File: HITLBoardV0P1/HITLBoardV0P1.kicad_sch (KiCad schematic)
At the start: 2 parts

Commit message: ADD SOLENOID VALVE CIRCUIT
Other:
- added sheet Solenoid-Valve (SolenoidValve.kicad_sch)
- added sheet Solenoid-Valve1 (SolenoidValve.kicad_sch)
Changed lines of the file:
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@@
 	(wire
 		(pts
+			(xy 513.08 213.36) (xy 537.21 213.36)
+		)
+		(stroke
+			(width 0)
+			(type default)
+		)
+	)
+	(wire
+		(pts
+			(xy 226.06 165.1) (xy 248.92 165.1)
+		)
+		(stroke
+			(width 0)
+			(type default)
+		)
+	)
+	(wire
+		(pts
 			(xy 381 317.5) (xy 403.86 317.5)
 		)
@@
 	(wire
 		(pts
+			(xy 167.64 209.55) (xy 187.96 209.55)
+		)
+		(stroke
+			(width 0)
+			(type default)
+		)
+	)
+	(wire
+		(pts
 			(xy 387.35 49.53) (xy 406.4 49.53)
 		)
@@
 	(wire
 		(pts
+			(xy 93.98 133.35) (xy 114.3 133.35)
+		)
+		(stroke
+			(width 0)
+			(type default)
+		)
+	)
+	(wire
+		(pts
 			(xy 290.83 303.53) (xy 314.96 303.53)
 		)
@@
 	(wire
 		(pts
+			(xy 226.06 209.55) (xy 248.92 209.55)
+		)
+		(stroke
+			(width 0)
+			(type default)
+		)
+	)
+	(wire
+		(pts
 			(xy 433.07 68.58) (xy 457.2 68.58)
 		)
@@
 	(wire
 		(pts
+			(xy 167.64 165.1) (xy 187.96 165.1)
+		)
+		(stroke
+			(width 0)
+			(type default)
+		)
+	)
+	(wire
+		(pts
 			(xy 130.81 330.2) (xy 149.86 330.2)
 		)
@@
 		)
 	)
+	(label "SV_ON_1"
+		(at 519.43 213.36 0)
+		(effects
+			(font
+				(size 1.27 1.27)
+			)
+			(justify left bottom)
+		)
+	)
 	(label "LAN_WAKE_1"
 		(at 438.15 73.66 0)
@@
 		)
 	)
+	(label "SV_EN_1"
+		(at 171.45 209.55 0)
+		(effects
+			(font
+				(size 1.27 1.27)
+			)
+			(justify left bottom)
+		)
+	)
 	(label "LAN1_RESET_N"
 		(at 307.34 53.34 0)
@@
 		)
 	)
+	(label "SV_EN_1"
+		(at 97.79 133.35 0)
+		(effects
+			(font
+				(size 1.27 1.27)
+			)
+			(justify left bottom)
+		)
+	)
 	(label "DAC_CLR3"
 		(at 476.25 321.31 90)
@@
 		)
 	)
+	(label "SV_ON_1"
+		(at 232.41 209.55 0)
+		(effects
+			(font
+				(size 1.27 1.27)
+			)
+			(justify left bottom)
+		)
+	)
 	(label "RPI_I2C_SCL"
 		(at 440.69 209.55 0)
@@
 		)
 	)
+	(label "SV_ON_1"
+		(at 232.41 165.1 0)
+		(effects
+			(font
+				(size 1.27 1.27)
+			)
+			(justify left bottom)
+		)
+	)
 	(label "RPI_SPI1_MOSI"
 		(at 215.9 340.36 0)
@@
 		)
 	)
+	(label "SV_EN_1"
+		(at 171.45 165.1 0)
+		(effects
+			(font
+				(size 1.27 1.27)
+			)
+			(justify left bottom)
+		)
+	)
 	(label "TMDX_SPI1_CS0_N"
 		(at 99.06 69.85 0)
@@
 	)
 	(sheet
+		(at 187.96 146.05)
+		(size 38.1 36.83)
+		(exclude_from_sim no)
+		(in_bom yes)
+		(on_board yes)
+		(dnp no)
+		(fields_autoplaced yes)
+		(stroke
+			(width 0.1524)
+			(type solid)
+		)
+		(fill
+			(color 0 0 0 0)
+		)
+		(property "Sheetname" "Solenoid-Valve"
+			(at 187.96 145.3384 0)
+			(show_name no)
+			(do_not_autoplace no)
+			(effects
+				(font
+					(size 1.27 1.27)
+				)
+				(justify left bottom)
+			)
+		)
+		(property "Sheetfile" "SolenoidValve.kicad_sch"
+			(at 187.96 183.4646 0)
+			(show_name no)
+			(do_not_autoplace no)
+			(effects
+				(font
+					(size 1.27 1.27)
+				)
+				(justify left top)
+			)
+		)
+		(pin "SV_EN_3V3" input
+			(at 187.96 165.1 180)
+			(effects
+				(font
+					(size 1.27 1.27)
+				)
+				(justify left)
+			)
+		)
+		(pin "SV_ON_3V3" input
+			(at 226.06 165.1 0)
+			(effects
+				(font
+					(size 1.27 1.27)
+				)
+				(justify right)
+			)
+		)
+		(instances
+			(project "HITLBoardV0P1"
+				(path "/ef043e91-6391-40b5-b326-2e3f2f5d4c07"
+					(page "14")
+				)
+			)
+		)
+	)
+	(sheet
 		(at 382.27 328.93)
 		(size 129.54 38.1)
@@
 				)
 			)
+		)
+	)
+	(sheet
+		(at 187.96 190.5)
+		(size 38.1 36.83)
+		(exclude_from_sim no)
+		(in_bom yes)
+		(on_board yes)
+		(dnp no)
+		(fields_autoplaced yes)
+		(stroke
+			(width 0.1524)
+			(type solid)
+		)
+		(fill
+			(color 0 0 0 0)
+		)
+		(property "Sheetname" "Solenoid-Valve1"
+			(at 187.96 189.7884 0)
+			(show_name no)
+			(do_not_autoplace no)
+			(effects
+				(font
+					(size 1.27 1.27)
+				)
+				(justify left bottom)
+			)
+		)
+		(property "Sheetfile" "SolenoidValve.kicad_sch"
+			(at 187.96 227.9146 0)
+			(show_name no)
+			(do_not_autoplace no)
+			(effects
+				(font
+					(size 1.27 1.27)
+				)
+				(justify left top)
+			)
+		)
+		(pin "SV_EN_3V3" input
+			(at 187.96 209.55 180)
+			(effects
+				(font
+					(size 1.27 1.27)
+				)
+				(justify left)
+			)
+		)
+		(pin "SV_ON_3V3" input
+			(at 226.06 209.55 0)
+			(effects
+				(font
+					(size 1.27 1.27)
+				)
+				(justify right)
+			)
+		)
+		(instances
+			(project "HITLBoardV0P1"
+				(path "/ef043e91-6391-40b5-b326-2e3f2f5d4c07"
+					(page "15")
+				)
+			)

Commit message: add debug LEDs and reset_n button for system reset
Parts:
- added R83: 10K, Resistor_SMD:R_01005_0402Metric, symbol Device:R_US
- added SW1: SW_Push, Button_Switch_SMD:SW_Push_1P1T_NO_E-Switch_TL3301NxxxxxG, symbol Switch:SW_Push
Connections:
- net +3.3VP: now also R83.1
- new net GND: SW1.2
- new net RESET_N: R83.2, SW1.1
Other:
- added sheet LEDs (LEDS.kicad_sch)
- sheet I2C_GPIO_EXPANDER ports: added RESET_N; removed none
- sheet RaspberryPiPico ports: added RESET_N; removed none
- sheet TMDX_Breakout ports: added GIOB_7, POR_RESET_N, SPI5_CS0_N, SPI5_CS1_NR, SPI5_SCLK, SPI5_SIMO_0, SPI5_SOMI_0; removed none
- moved on the sheet: R69, R70

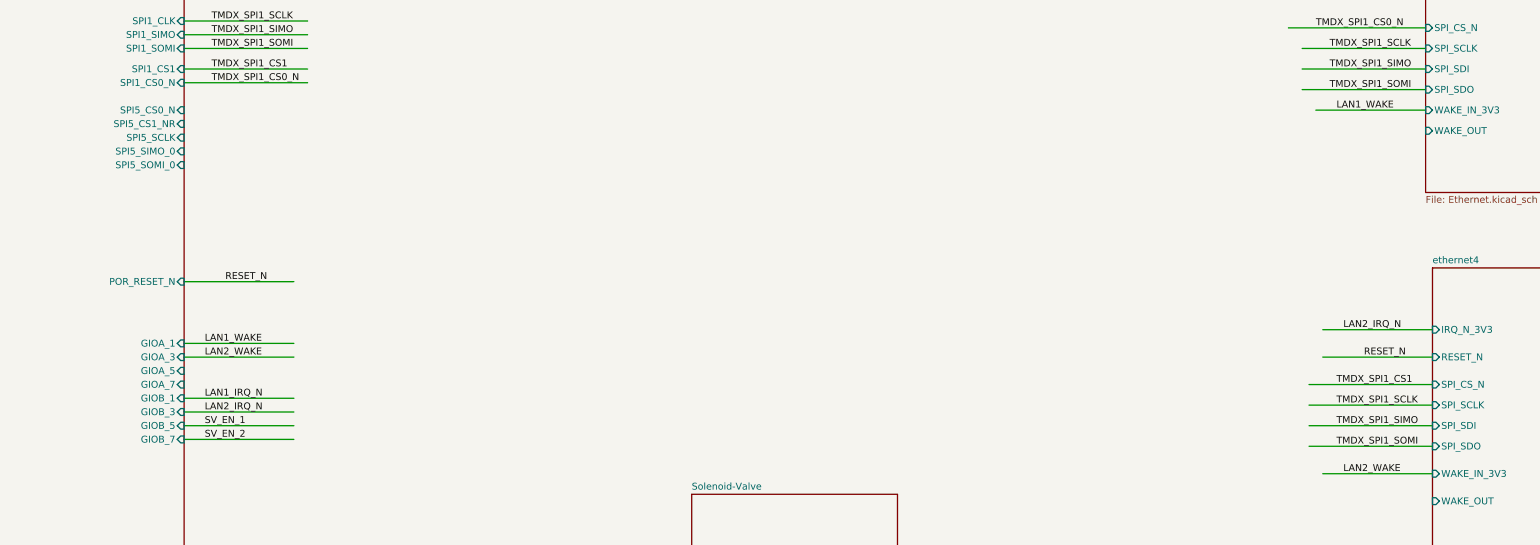
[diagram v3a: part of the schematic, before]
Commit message: MINOR UPDATES -- SWTICH ONE LAN TO SPI 5 INSTEAD OF SPI1 ON THE TMDX, SET UP LAN8650S for actual differential pair routing by changing suffix to "_DN" and "_DP" instead of "_N" or "_P" or just "N", "P"
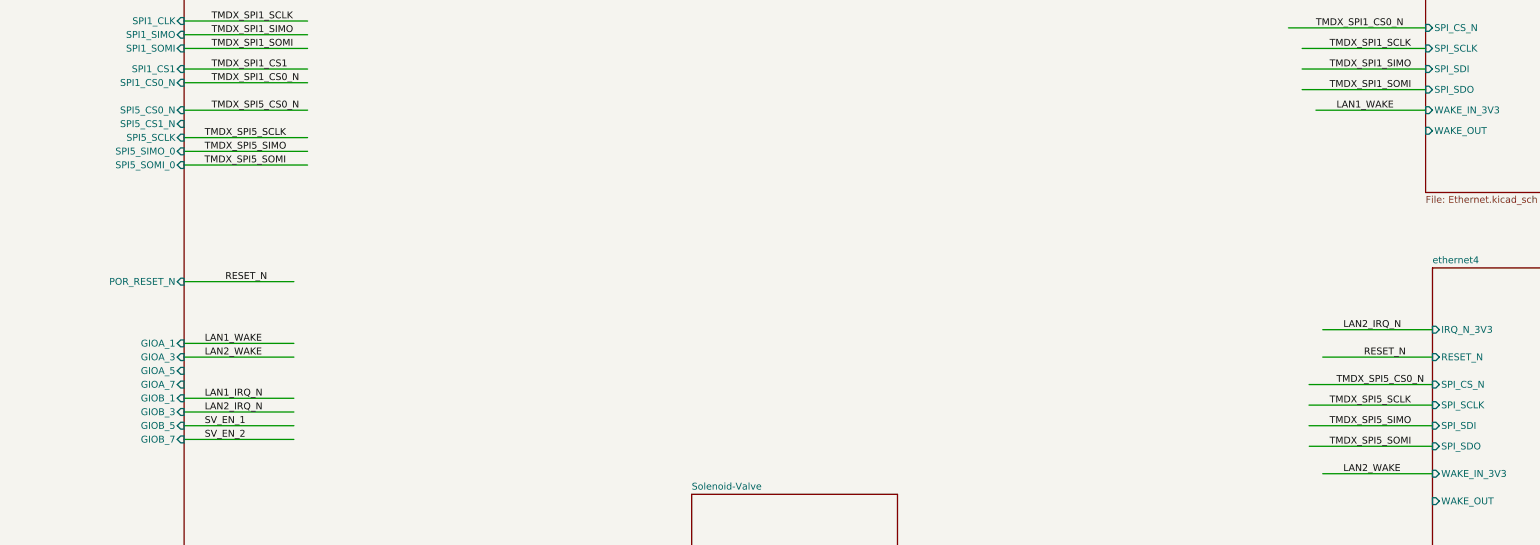
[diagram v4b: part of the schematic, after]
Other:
- sheet TMDX_Breakout ports: added SPI5_CS1_N; removed SPI5_CS1_NR
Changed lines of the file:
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@@
 	(wire
 		(pts
+			(xy 93.98 85.09) (xy 116.84 85.09)
+		)
+		(stroke
+			(width 0)
+			(type default)
+		)
+	)
+	(wire
+		(pts
 			(xy 461.01 304.8) (xy 461.01 328.93)
 		)
@@
 	(wire
 		(pts
+			(xy 302.26 133.35) (xy 325.12 133.35)
+		)
+		(stroke
+			(width 0)
+			(type default)
+		)
+	)
+	(wire
+		(pts
 			(xy 130.81 337.82) (xy 149.86 337.82)
 		)
@@
 	(wire
 		(pts
-			(xy 302.26 129.54) (xy 325.12 129.54)
-		)
-		(stroke
-			(width 0)
-			(type default)
-		)
-	)
-	(wire
-		(pts
 			(xy 130.81 322.58) (xy 149.86 322.58)
 		)
@@
 	(wire
 		(pts
-			(xy 302.26 133.35) (xy 325.12 133.35)
+			(xy 93.98 82.55) (xy 116.84 82.55)
 		)
 		(stroke
@@
 	(wire
 		(pts
-			(xy 302.26 125.73) (xy 325.12 125.73)
+			(xy 93.98 199.39) (xy 118.11 199.39)
 		)
 		(stroke
@@
 	(wire
 		(pts
-			(xy 93.98 199.39) (xy 118.11 199.39)
+			(xy 77.47 318.77) (xy 96.52 318.77)
 		)
 		(stroke
@@
 	(wire
 		(pts
-			(xy 77.47 318.77) (xy 96.52 318.77)
+			(xy 511.81 290.83) (xy 490.22 290.83)
 		)
 		(stroke
@@
 	(wire
 		(pts
-			(xy 511.81 290.83) (xy 490.22 290.83)
+			(xy 449.58 304.8) (xy 449.58 328.93)
 		)
 		(stroke
@@
 	(wire
 		(pts
-			(xy 449.58 304.8) (xy 449.58 328.93)
+			(xy 415.29 304.8) (xy 415.29 328.93)
 		)
 		(stroke
@@
 	(wire
 		(pts
-			(xy 415.29 304.8) (xy 415.29 328.93)
+			(xy 518.16 123.19) (xy 537.21 123.19)
 		)
 		(stroke
@@
 	(wire
 		(pts
-			(xy 518.16 123.19) (xy 537.21 123.19)
+			(xy 302.26 129.54) (xy 325.12 129.54)
 		)
 		(stroke
@@
 	(wire
 		(pts
+			(xy 93.98 80.01) (xy 116.84 80.01)
+		)
+		(stroke
+			(width 0)
+			(type default)
+		)
+	)
+	(wire
+		(pts
 			(xy 262.89 337.82) (xy 281.94 337.82)
 		)
@@
 	(wire
 		(pts
+			(xy 302.26 125.73) (xy 325.12 125.73)
+		)
+		(stroke
+			(width 0)
+			(type default)
+		)
+	)
+	(wire
+		(pts
 			(xy 93.98 133.35) (xy 114.3 133.35)
 		)
@@
 	(wire
 		(pts
+			(xy 93.98 74.93) (xy 116.84 74.93)
+		)
+		(stroke
+			(width 0)
+			(type default)
+		)
+	)
+	(wire
+		(pts
 			(xy 403.86 328.93) (xy 403.86 317.5)
 		)
@@
 	(wire
 		(pts
-			(xy 212.2657 344.0949) (xy 236.3957 344.0949)
+			(xy 302.312 137.16) (xy 325.12 137.16)
 		)
 		(stroke
@@
 	(wire
 		(pts
-			(xy 290.83 331.47) (xy 314.96 331.47)
+			(xy 212.2657 344.0949) (xy 236.3957 344.0949)
 		)
 		(stroke
@@
 	(wire
 		(pts
-			(xy 433.07 60.96) (xy 457.2 60.96)
+			(xy 290.83 331.47) (xy 314.96 331.47)
 		)
 		(stroke
@@
 	(wire
 		(pts
-			(xy 290.83 340.36) (xy 314.96 340.36)
+			(xy 433.07 60.96) (xy 457.2 60.96)
 		)
 		(stroke
@@
 	(wire
 		(pts
-			(xy 290.83 307.34) (xy 314.96 307.34)
+			(xy 290.83 340.36) (xy 314.96 340.36)
 		)
 		(stroke
@@
 	(wire
 		(pts
-			(xy 93.98 196.85) (xy 118.11 196.85)
+			(xy 290.83 307.34) (xy 314.96 307.34)
 		)
 		(stroke
@@
 	(wire
 		(pts
-			(xy 302.26 137.16) (xy 325.12 137.16)
+			(xy 93.98 196.85) (xy 118.11 196.85)
 		)
 		(stroke
@@
 		)
 	)
+	(label "TMDX_SPI5_SIMO"
+		(at 97.79 82.55 0)
+		(effects
+			(font
+				(size 1.27 1.27)
+			)
+			(justify left bottom)
+		)
+	)
 	(label "I_LOOP_4"
 		(at 346.71 336.55 0)
@@
 		)
 	)
+	(label "TMDX_SPI5_SOMI"
+		(at 306.07 137.16 0)
+		(effects
+			(font
+				(size 1.27 1.27)
+			)
+			(justify left bottom)
+		)
+	)
 	(label "IRQ_N_0"
 		(at 441.96 116.84 0)
@@
 		)
 	)
-	(label "TMDX_SPI1_SOMI"
-		(at 307.34 137.16 0)
+	(label "DAC_CLR2"
+		(at 457.2 321.31 90)
 		(effects
 			(font
@@
 		)
 	)
-	(label "DAC_CLR2"
-		(at 457.2 321.31 90)
+	(label "RPI_SPI1_SCK"
+		(at 215.9 344.17 0)
 		(effects
 			(font
@@
 		)
 	)
-	(label "RPI_SPI1_SCK"
-		(at 215.9 344.17 0)
+	(label "TMDX_SPI5_SCLK"
+		(at 306.07 129.54 0)
 		(effects
 			(font
@@
 		)
 	)
-	(label "TMDX_SPI1_SIMO"
-		(at 307.34 133.35 0)
-		(effects
-			(font
-				(size 1.27 1.27)
-			)
-			(justify left bottom)
-		)
-	)
 	(label "DAC_CLR1"
 		(at 228.6 332.74 180)
@@
 		)
 	)
+	(label "TMDX_SPI5_SOMI"
+		(at 97.738 85.09 0)
+		(effects
+			(font
+				(size 1.27 1.27)
+			)
+			(justify left bottom)
+		)
+	)
 	(label "RPI_UART1_TX"
 		(at 480.06 321.31 90)
@@
 		)
 	)
-	(label "TMDX_SPI1_SCLK"
-		(at 307.34 129.54 0)
-		(effects
-			(font
-				(size 1.27 1.27)
-			)
-			(justify left bottom)
-		)
-	)
 	(label "TMDX_SPI1_CS1"
 		(at 99.06 67.31 0)
@@
 		)
 	)
-	(label "TMDX_SPI1_CS1"
-		(at 307.34 125.73 0)
-		(effects
-			(font
-				(size 1.27 1.27)
-			)
-			(justify left bottom)
-		)
-	)
 	(label "LAN_WAKE_0"
 		(at 449.58 142.24 180)
@@
 		)
 	)
+	(label "TMDX_SPI5_SCLK"
+		(at 97.79 80.01 0)
+		(effects
+			(font
+				(size 1.27 1.27)
+			)
+			(justify left bottom)
+		)
+	)
 	(label "I_LOOP_2"
 		(at 82.55 318.77 0)
@@
 		)
 	)
+	(label "TMDX_SPI5_SIMO"
+		(at 306.07 133.35 0)
+		(effects
+			(font
+				(size 1.27 1.27)
+			)
+			(justify left bottom)
+		)
+	)
 	(label "RESET_N"
 		(at 311.15 53.34 0)
@@
 		)
 	)
+	(label "TMDX_SPI5_CS0_N"
+		(at 307.34 125.73 0)
+		(effects
+			(font
+				(size 1.27 1.27)
+			)
+			(justify left bottom)
+		)
+	)
 	(label "RPI_SPI1_MISO"
 		(at 217.1643 346.71 0)
@@
 		)
 	)
+	(label "TMDX_SPI5_CS0_N"
+		(at 99.06 74.93 0)
+		(effects
+			(font
+				(size 1.27 1.27)
+			)
+			(justify left bottom)
+		)
+	)
 	(label "IRQ_N_1"
 		(at 440.69 46.99 0)
@@
 			)
 		)
-		(pin "SPI5_CS1_NR" input
+		(pin "SPI5_CS1_N" input
 			(at 93.98 77.47 0)
 			(effects
